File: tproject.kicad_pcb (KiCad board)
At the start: 2 copper layers, 0 parts

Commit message: Place all 26 components on PCB (initial floorplan) and add design note 0009
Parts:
- added C1: 22u, Capacitor_SMD:C_0805_2012Metric, F.Cu at (124.5, 44.4)
- added C10: 1u, Capacitor_SMD:C_0402_1005Metric, F.Cu at (49.3, 73.6)
- added C11: 100n, Capacitor_SMD:C_0402_1005Metric, F.Cu at (125.5, 71.0)
- added C12: 10p, Capacitor_SMD:C_0402_1005Metric, F.Cu at (47.8, 66.0)
- added C13: 10p, Capacitor_SMD:C_0402_1005Metric, F.Cu at (47.8, 68.8)
- added C2: 22u, Capacitor_SMD:C_0805_2012Metric, F.Cu at (124.5, 47.4)
- added C3: 10u, Capacitor_SMD:C_0603_1608Metric, F.Cu at (118.6, 67.7)
- added C4: 100n, Capacitor_SMD:C_0402_1005Metric, F.Cu at (50.0, 63.0)
- added C5: 100n, Capacitor_SMD:C_0402_1005Metric, F.Cu at (122.7, 66.0)
- added C6: 100n, Capacitor_SMD:C_0402_1005Metric, F.Cu at (122.7, 71.0)
- added C7: 100n, Capacitor_SMD:C_0402_1005Metric, F.Cu at (53.5, 60.0)
- added C8: 10n, Capacitor_SMD:C_0402_1005Metric, F.Cu at (49.8, 67.5)
- added C9: 1u, Capacitor_SMD:C_0402_1005Metric, F.Cu at (49.3, 72.1)
- added D1: RED, LED_SMD:LED_0603_1608Metric, F.Cu at (124.3, 50.2)
- added FB1: 120R, Inductor_SMD:L_0603_1608Metric, F.Cu at (51.2, 72.5)
- added J1: USB_B_Micro, Connector_USB:USB_Micro-B_Wuerth_629105150521, F.Cu at (116.8, 46.7)
- added J2: Conn_01x04_Pin, Connector_PinHeader_1.00mm:PinHeader_1x04_P1.00mm_Vertical_SMD_Pin1Right, F.Cu at (114.1, 55.1)
- added J3: Conn_01x04_Pin, Connector_PinHeader_1.00mm:PinHeader_1x04_P1.00mm_Vertical_SMD_Pin1Right, F.Cu at (119.7, 55.1)
- added J4: Conn_01x04_Pin, Connector_PinHeader_1.00mm:PinHeader_1x04_P1.00mm_Vertical_SMD_Pin1Right, F.Cu at (125.2, 55.1)
- added R1: 1k5, Resistor_SMD:R_0402_1005Metric, F.Cu at (108.5, 61.7)
- added R2: 10k, Resistor_SMD:R_0402_1005Metric, F.Cu at (108.5, 63.7)
- added R3: 1k5, Resistor_SMD:R_0402_1005Metric, F.Cu at (108.5, 65.7)
- added R4: 1k5, Resistor_SMD:R_0402_1005Metric, F.Cu at (108.5, 67.7)
- added R5: 1k5, Resistor_SMD:R_0402_1005Metric, F.Cu at (39.7, 68.3)
- added SW1: SW_SPDT, Button_Switch_THT:SW_E-Switch_EG1224_SPDT_Angled, F.Cu at (99.6, 46.5)
- added U1: STM32F103C8T6, Package_QFP:LQFP-48_7x7mm_P0.5mm, F.Cu at (56.0, 67.2)
- added U2: AMS1117-3.3, Package_TO_SOT_SMD:SOT-223-3_TabPin2, F.Cu at (116.3, 62.3)
- added Y1: 16MHz, Crystal:Crystal_SMD_3225-4Pin_3.2x2.5mm, F.Cu at (45.0, 67.4)

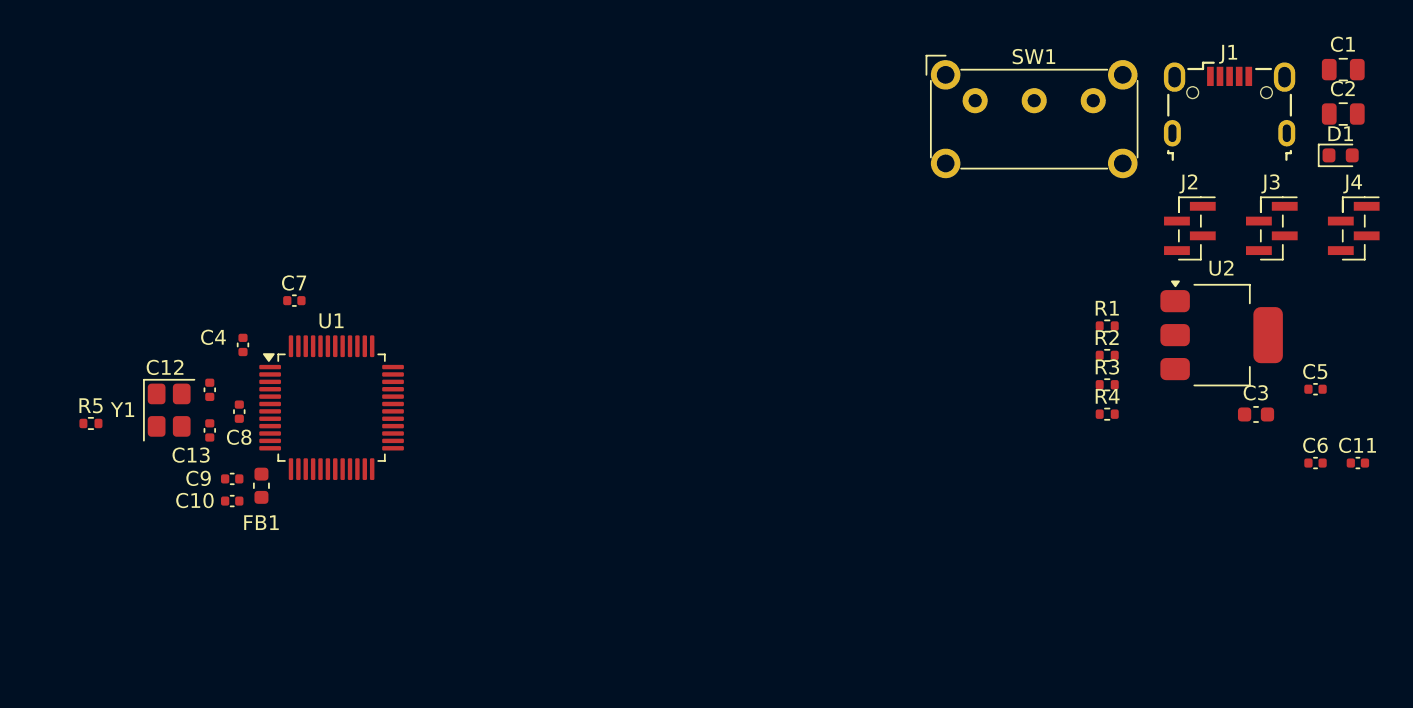
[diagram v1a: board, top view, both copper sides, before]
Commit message: Refine USB and SWD/SWO circuit component placement and add design note 0010
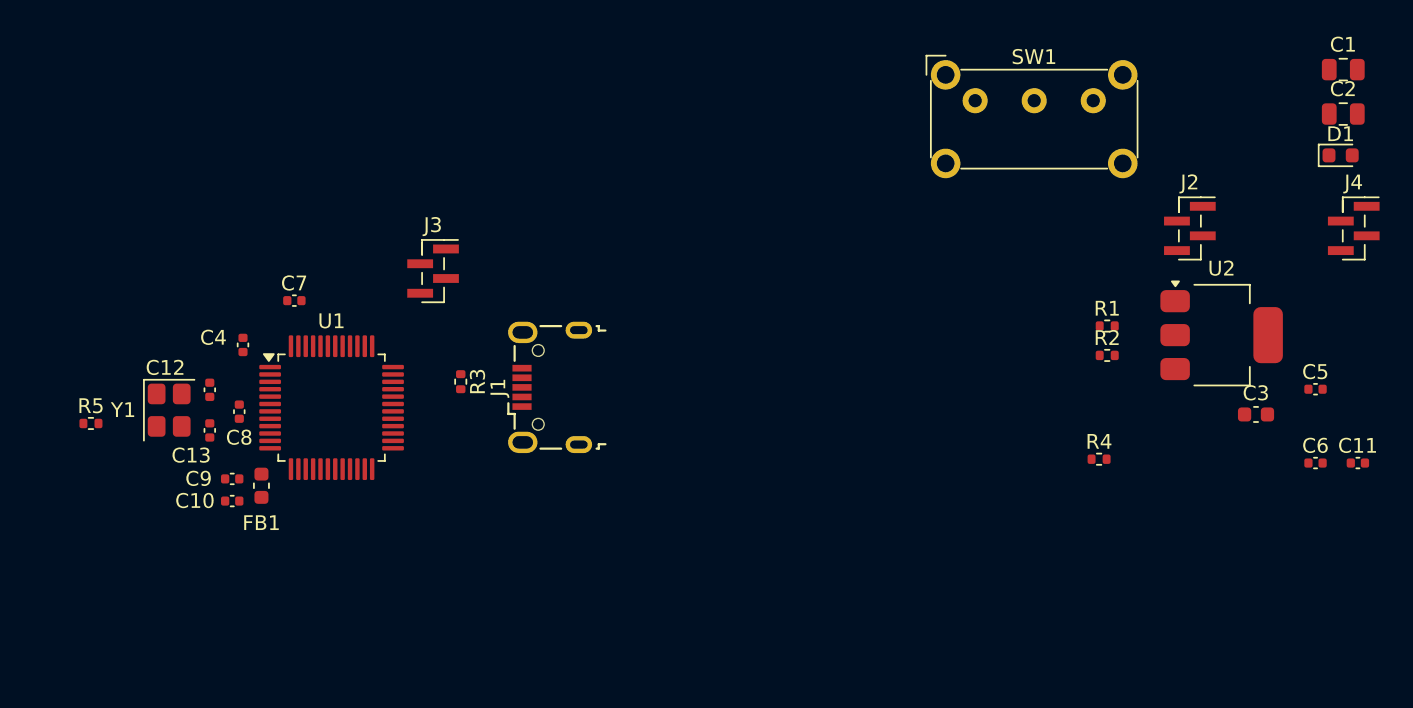
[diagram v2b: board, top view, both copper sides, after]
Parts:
- moved J3 56.9 mm to (62.9, 58.0)
- moved J1 49.9 mm to (70.8, 65.9), turned to 90 degrees
- moved R3 43.8 mm to (64.8, 65.5), turned to -90 degrees
- moved R4 3.10 mm to (108.0, 70.7)
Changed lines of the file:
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@@
 	(footprint "Resistor_SMD:R_0402_1005Metric"
 		(layer "F.Cu")
-		(at 108.54 67.69)
+		(at 107.99 70.74)
 		(descr "Resistor SMD 0402 (1005 Metric), square (rectangular) end terminal, IPC-7351 nominal, (Body size source: IPC-SM-782 page 72, https://www.pcb-3d.com/wordpress/wp-content/uploads/ipc-sm-782a_amendment_1_and_2.pdf), generated with kicad-footprint-generator")
 		(tags "resistor")
@@
 	(footprint "Connector_PinHeader_1.00mm:PinHeader_1x04_P1.00mm_Vertical_SMD_Pin1Right"
 		(layer "F.Cu")
-		(at 119.69 55.11)
+		(at 62.875 58)
 		(descr "surface-mounted straight pin header, 1x04, 1.00mm pitch, single row, style 2 (pin 1 right)")
 		(tags "Surface mounted pin header SMD 1x04 1.00mm single row style2 pin1 right")
@@
 	(footprint "Resistor_SMD:R_0402_1005Metric"
 		(layer "F.Cu")
-		(at 108.54 65.7)
+		(at 64.75 65.49 -90)
 		(descr "Resistor SMD 0402 (1005 Metric), square (rectangular) end terminal, IPC-7351 nominal, (Body size source: IPC-SM-782 page 72, https://www.pcb-3d.com/wordpress/wp-content/uploads/ipc-sm-782a_amendment_1_and_2.pdf), generated with kicad-footprint-generator")
 		(tags "resistor")
 		(property "Reference" "R3"
-			(at 0 -1.17 0)
+			(at 0 -1.17 90)
 			(layer "F.SilkS")
 			(effects
@@
 		)
 		(property "Value" "1k5"
-			(at 0 1.17 0)
+			(at 0 1.17 90)
 			(layer "F.Fab")
 			(effects
@@
 		)
 		(property "Datasheet" "~"
-			(at 0 0 0)
+			(at 0 0 90)
 			(layer "F.Fab")
 			(hide yes)
@@
 		)
 		(property "Description" "Resistor"
-			(at 0 0 0)
+			(at 0 0 90)
 			(layer "F.Fab")
 			(hide yes)
@@
 		(attr smd)
 		(fp_line
-			(start -0.153641 -0.38)
-			(end 0.153641 -0.38)
+			(start -0.153641 0.38)
+			(end 0.153641 0.38)
 			(stroke
 				(width 0.12)
@@
 		)
 		(fp_line
-			(start -0.153641 0.38)
-			(end 0.153641 0.38)
+			(start -0.153641 -0.38)
+			(end 0.153641 -0.38)
 			(stroke
 				(width 0.12)
@@
 		)
 		(fp_text user "${REFERENCE}"
-			(at 0 0 0)
+			(at 0 0 90)
 			(layer "F.Fab")
 			(effects
@@
 		)
 		(pad "1" smd roundrect
-			(at -0.51 0)
+			(at -0.51 0 270)
 			(size 0.54 0.64)
 			(layers "F.Cu" "F.Mask" "F.Paste")
@@
 		)
 		(pad "2" smd roundrect
-			(at 0.51 0)
+			(at 0.51 0 270)
 			(size 0.54 0.64)
 			(layers "F.Cu" "F.Mask" "F.Paste")
@@
 	(footprint "Connector_USB:USB_Micro-B_Wuerth_629105150521"
 		(layer "F.Cu")
-		(at 116.83 46.71)
+		(at 70.8 65.875 90)
 		(descr "USB Micro-B receptacle, http://www.mouser.com/ds/2/445/629105150521-469306.pdf")
 		(tags "usb micro receptacle")
 		(property "Reference" "J1"
-			(at 0 -3.5 0)
+			(at 0 -3.5 90)
 			(layer "F.SilkS")
 			(effects
@@
 		)
 		(property "Value" "USB_B_Micro"
-			(at 0 5.6 0)
+			(at 0 5.6 90)
 			(layer "F.Fab")
 			(effects
@@
 		)
 		(property "Datasheet" "~"
-			(at 0 0 0)
+			(at 0 0 90)
 			(unlocked yes)
 			(layer "F.Fab")
@@
 		)
 		(property "Description" "USB Micro Type B connector"
-			(at 0 0 0)
+			(at 0 0 90)
 			(unlocked yes)
 			(layer "F.Fab")
@@
 		(attr smd)
 		(fp_line
-			(start -4.15 -0.65)
-			(end -4.15 0.75)
+			(start -1.075 -2.825)
+			(end -1.8 -2.825)
 			(stroke
 				(width 0.15)
@@
 		)
 		(fp_line
-			(start -4.15 3.15)
-			(end -4.15 3.3)
+			(start -1.8 -2.825)
+			(end -1.8 -2.4)
 			(stroke
 				(width 0.15)
@@
 		)
 		(fp_line
-			(start -4.15 3.3)
-			(end -3.85 3.3)
+			(start 1.8 -2.4)
+			(end 2.8 -2.4)
 			(stroke
 				(width 0.15)
@@
 		)
 		(fp_line
-			(start -3.85 3.3)
-			(end -3.85 3.75)
+			(start -1.8 -2.4)
+			(end -2.8 -2.4)
 			(stroke
 				(width 0.15)
@@
 		)
 		(fp_line
-			(start -1.8 -2.825)
-			(end -1.8 -2.4)
+			(start -4.15 -0.65)
+			(end -4.15 0.75)
 			(stroke
 				(width 0.15)
@@
 		)
 		(fp_line
-			(start -1.8 -2.4)
-			(end -2.8 -2.4)
+			(start 4.15 0.75)
+			(end 4.15 -0.65)
 			(stroke
 				(width 0.15)
@@
 		)
 		(fp_line
-			(start -1.075 -2.825)
-			(end -1.8 -2.825)
+			(start -4.15 3.15)
+			(end -4.15 3.3)
 			(stroke
 				(width 0.15)
@@
 		)
 		(fp_line
-			(start 1.8 -2.4)
-			(end 2.8 -2.4)
+			(start 4.15 3.3)
+			(end 4.15 3.15)
 			(stroke
 				(width 0.15)
@@
 		)
 		(fp_line
-			(start 3.85 3.75)
-			(end 3.85 3.3)
+			(start -3.85 3.3)
+			(end -3.85 3.75)
 			(stroke
 				(width 0.15)
@@
 		)
 		(fp_line
-			(start 4.15 0.75)
-			(end 4.15 -0.65)
+			(start -4.15 3.3)
+			(end -3.85 3.3)
 			(stroke
 				(width 0.15)
@@
 		)
 		(fp_line
-			(start 4.15 3.3)
-			(end 4.15 3.15)
+			(start 3.85 3.75)
+			(end 3.85 3.3)
 			(stroke
 				(width 0.15)
@@
 		)
 		(fp_line
-			(start -4.94 -3.34)
-			(end -4.94 4.85)
+			(start 4.95 -3.34)
+			(end -4.94 -3.34)
 			(stroke
 				(width 0.05)
@@
 		)
 		(fp_line
-			(start -4.94 4.85)
-			(end 4.95 4.85)
+			(start -4.94 -3.34)
+			(end -4.94 4.85)
 			(stroke
 				(width 0.05)
@@
 		)
 		(fp_line
-			(start 4.95 -3.34)
-			(end -4.94 -3.34)
+			(start 4.95 4.85)
+			(end 4.95 -3.34)
 			(stroke
 				(width 0.05)
@@
 		)
 		(fp_line
-			(start 4.95 4.85)
-			(end 4.95 -3.34)
+			(start -4.94 4.85)
+			(end 4.95 4.85)
 			(stroke
 				(width 0.05)
@@
 		)
 		(fp_line
-			(start -4 -2.25)
-			(end -4 3.15)
+			(start -1.075 -2.95)
+			(end -1.075 -2.725)
 			(stroke
 				(width 0.15)
@@
 		)
 		(fp_line
-			(start -4 3.15)
-			(end -3.7 3.15)
+			(start -1.525 -2.95)
+			(end -1.075 -2.95)
 			(stroke
 				(width 0.15)
@@
 		)
 		(fp_line
-			(start -3.7 3.15)
-			(end -3.7 4.35)
+			(start -1.075 -2.725)
+			(end -1.3 -2.55)
 			(stroke
 				(width 0.15)
@@
 		)
 		(fp_line
-			(start -3.7 4.35)
-			(end 3.7 4.35)
+			(start -1.525 -2.725)
+			(end -1.525 -2.95)
 			(stroke
 				(width 0.15)
@@
 		)
 		(fp_line
-			(start -2.7 3.75)
-			(end 2.7 3.75)
+			(start -1.3 -2.55)
+			(end -1.525 -2.725)
 			(stroke
 				(width 0.15)
@@
 		)
 		(fp_line
-			(start -1.525 -2.95)
-			(end -1.075 -2.95)
+			(start 4 -2.25)
+			(end -4 -2.25)
 			(stroke
 				(width 0.15)
@@
 		)
 		(fp_line
-			(start -1.525 -2.725)
-			(end -1.525 -2.95)
+			(start -4 -2.25)
+			(end -4 3.15)
 			(stroke
 				(width 0.15)
@@
 		)
 		(fp_line
-			(start -1.3 -2.55)
-			(end -1.525 -2.725)
+			(start 4 3.15)
+			(end 4 -2.25)
 			(stroke
 				(width 0.15)
@@
 		)
 		(fp_line
-			(start -1.075 -2.95)
-			(end -1.075 -2.725)
+			(start 3.7 3.15)
+			(end 4 3.15)
 			(stroke
 				(width 0.15)
@@
 		)
 		(fp_line
-			(start -1.075 -2.725)
-			(end -1.3 -2.55)
+			(start -3.7 3.15)
+			(end -3.7 4.35)
 			(stroke
 				(width 0.15)
@@
 		)
 		(fp_line
-			(start 3.7 3.15)
-			(end 4 3.15)
+			(start -4 3.15)
+			(end -3.7 3.15)
 			(stroke
 				(width 0.15)
@@
 		)
 		(fp_line
-			(start 3.7 4.35)
-			(end 3.7 3.15)
+			(start -2.7 3.75)
+			(end 2.7 3.75)
 			(stroke
 				(width 0.15)
@@
 		)
 		(fp_line
-			(start 4 -2.25)
-			(end -4 -2.25)
+			(start 3.7 4.35)
+			(end 3.7 3.15)
 			(stroke
 				(width 0.15)
@@
 		)
 		(fp_line
-			(start 4 3.15)
-			(end 4 -2.25)
+			(start -3.7 4.35)
+			(end 3.7 4.35)
 			(stroke
 				(width 0.15)
@@
 		)
 		(fp_text user "PCB Edge"
-			(at 0 3.75 0)
+			(at 0 3.75 90)
 			(layer "Dwgs.User")
 			(effects
@@
 		)
 		(fp_text user "${REFERENCE}"
-			(at 0 1.05 0)
+			(at 0 1.05 90)
 			(layer "F.Fab")
 			(effects
@@
 		)
 		(pad "" np_thru_hole oval
-			(at -2.5 -0.8)
+			(at -2.5 -0.8 90)
 			(size 0.8 0.8)
 			(drill 0.8)
@@
 		)
 		(pad "" np_thru_hole oval
-			(at 2.5 -0.8)
+			(at 2.5 -0.8 90)
 			(size 0.8 0.8)
 			(drill 0.8)
@@
 		)
 		(pad "1" smd rect
-			(at -1.3 -1.9)
+			(at -1.3 -1.9 90)
 			(size 0.45 1.3)
 			(layers "F.Cu" "F.Mask" "F.Paste")
@@
 		)
 		(pad "2" smd rect
-			(at -0.65 -1.9)
+			(at -0.65 -1.9 90)
 			(size 0.45 1.3)
 			(layers "F.Cu" "F.Mask" "F.Paste")
@@
 		)
 		(pad "3" smd rect
-			(at 0 -1.9)
+			(at 0 -1.9 90)
 			(size 0.45 1.3)
 			(layers "F.Cu" "F.Mask" "F.Paste")
@@
 		)
 		(pad "4" smd rect
-			(at 0.65 -1.9)
+			(at 0.65 -1.9 90)
 			(size 0.45 1.3)
 			(layers "F.Cu" "F.Mask" "F.Paste")
@@
 		)
 		(pad "5" smd rect
-			(at 1.3 -1.9)
+			(at 1.3 -1.9 90)
 			(size 0.45 1.3)
 			(layers "F.Cu" "F.Mask" "F.Paste")
@@
 		)
 		(pad "6" thru_hole oval
-			(at -3.875 1.95)
+			(at -3.875 1.95 90)
 			(size 1.15 1.8)
 			(drill oval 0.55 1.2)
@@
 		)
 		(pad "6" thru_hole oval
-			(at -3.725 -1.85)
+			(at -3.725 -1.85 90)
 			(size 1.45 2)
 			(drill oval 0.85 1.4)
@@
 		)
 		(pad "6" thru_hole oval
-			(at 3.725 -1.85)
+			(at 3.725 -1.85 90)
 			(size 1.45 2)
 			(drill oval 0.85 1.4)
@@
 		)
 		(pad "6" thru_hole oval
-			(at 3.875 1.95)
+			(at 3.875 1.95 90)
 			(size 1.15 1.8)
 			(drill oval 0.55 1.2)

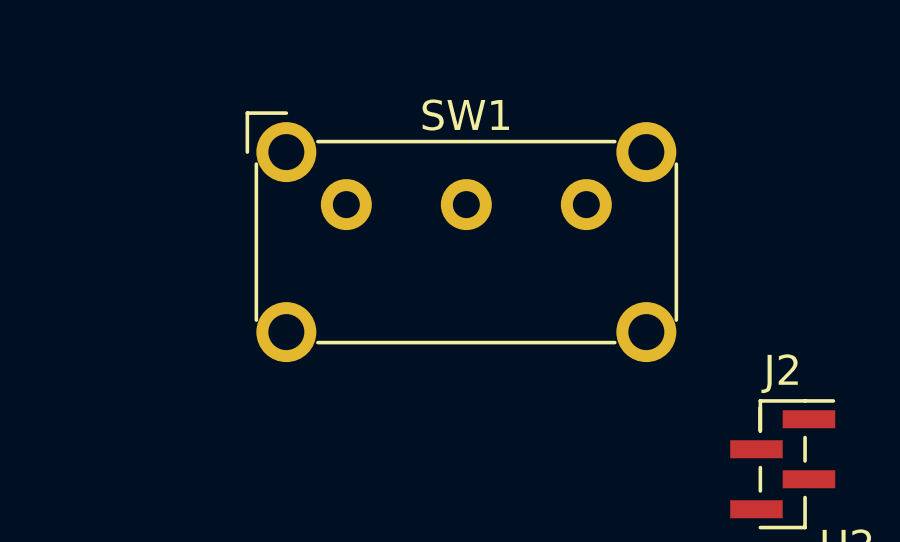
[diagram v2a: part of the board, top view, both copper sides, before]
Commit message: Replace SW1 with SMD PCM12 footprint, add Wurth USB STEP model, and add design note 0011
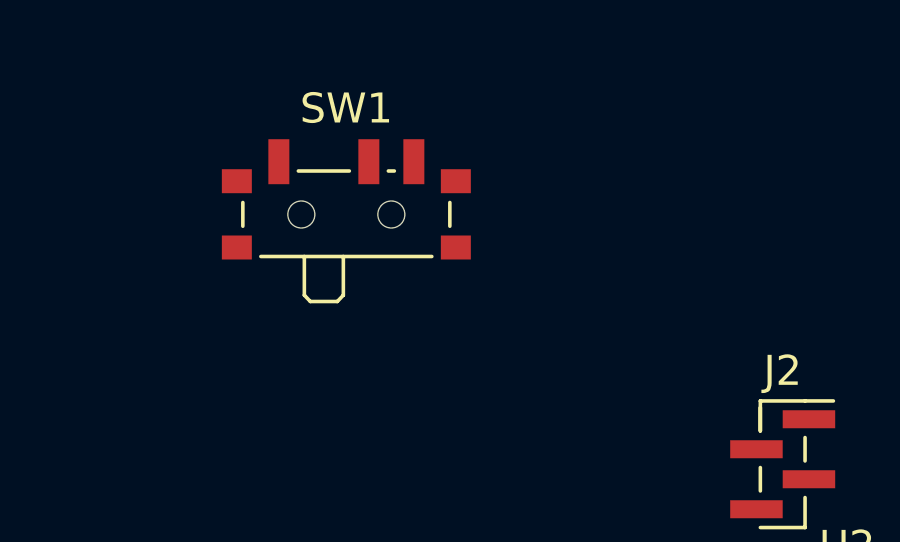
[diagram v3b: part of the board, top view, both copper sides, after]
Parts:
- SW1: footprint Button_Switch_THT:SW_E-Switch_EG1224_SPDT_Angled -> Button_Switch_SMD:SW_SPDT_PCM12

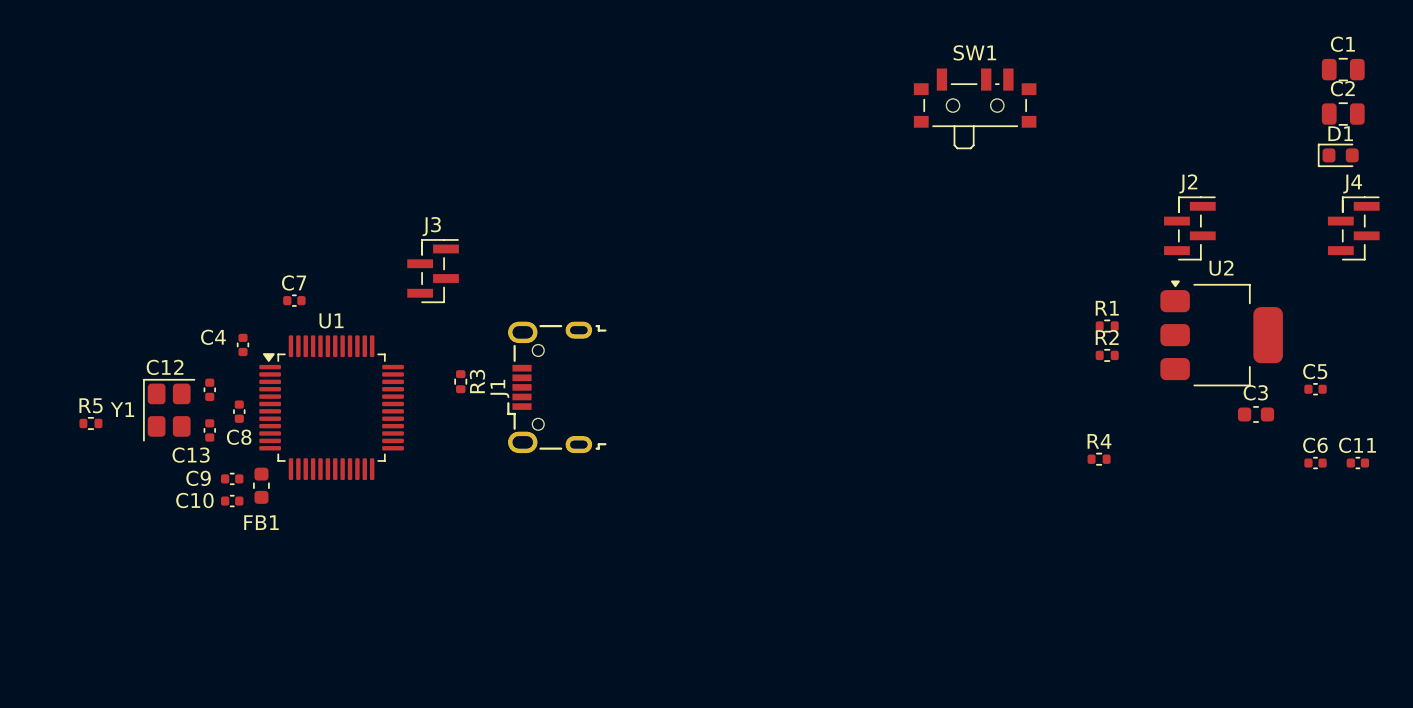
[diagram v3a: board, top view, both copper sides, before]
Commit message: Refine switch, connector, and peripheral circuit placement and add design note 0012
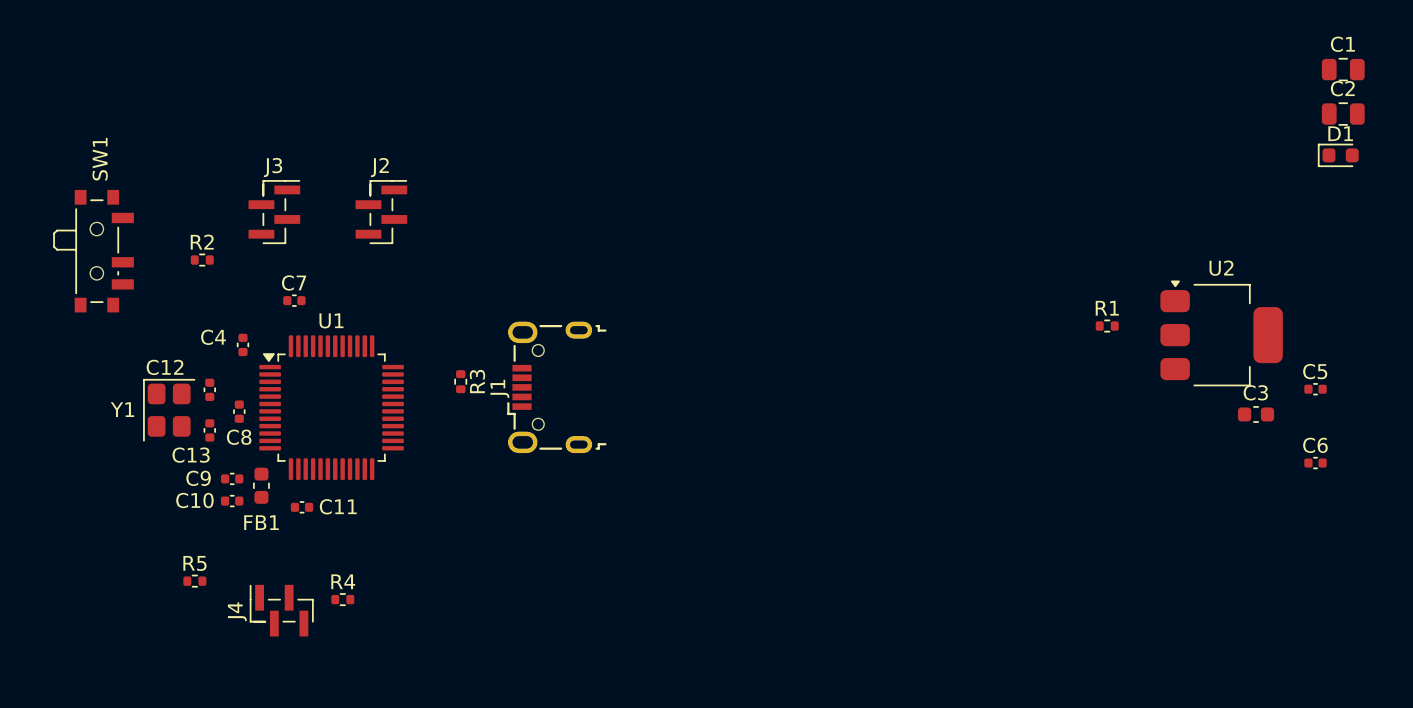
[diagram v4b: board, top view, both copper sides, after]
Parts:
- moved J4 77.1 mm to (52.6, 81.0), turned to 90 degrees
- moved C11 71.6 mm to (54.0, 74.0)
- moved R2 61.6 mm to (47.2, 57.2)
- moved SW1 60.0 mm to (40.4, 56.6), turned to -90 degrees
- moved J2 54.8 mm to (59.4, 54.0)
- moved R4 52.1 mm to (56.8, 80.2)
- moved R5 12.8 mm to (46.7, 79.0)
- moved J3 11.5 mm to (52.1, 54.0)

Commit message: Finalize power supply cluster placement (U2, C1-C3, C5-C7, D1, R1) and add design note 0013
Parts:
- moved C3 68.7 mm to (50.5, 59.0)
- moved C1 67.0 mm to (63.5, 72.0)
- moved C5 63.0 mm to (60.2, 75.0)
- moved C2 62.1 mm to (71.2, 79.2), turned to 90 degrees
- moved C6 59.9 mm to (63.0, 65.5), turned to 90 degrees
- moved D1 57.8 mm to (73.8, 78.0), turned to 90 degrees
- moved U2 53.4 mm to (65.5, 78.8), turned to -90 degrees
- moved R1 39.5 mm to (70.8, 73.2), turned to 90 degrees
- moved C7 1.23 mm to (52.5, 60.8)
